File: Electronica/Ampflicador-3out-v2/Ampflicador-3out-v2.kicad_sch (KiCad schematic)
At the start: 28 parts, among them Q1 MPF102, U1 LM386

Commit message: Amp v2
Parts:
- R1, R2, R3, R4, R5, R6: footprint Resistor_THT:R_Axial_DIN0204_L3.6mm_D1.6mm_P5.08mm_Horizontal -> Resistor_THT:R_Axial_DIN0204_L3.6mm_D1.6mm_P7.62mm_Horizontal
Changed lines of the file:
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@@
 			)
 		)
-		(property "Footprint" "Resistor_THT:R_Axial_DIN0204_L3.6mm_D1.6mm_P5.08mm_Horizontal"
+		(property "Footprint" "Resistor_THT:R_Axial_DIN0204_L3.6mm_D1.6mm_P7.62mm_Horizontal"
 			(at 101.346 99.314 90)
 			(effects
@@
 			)
 		)
-		(property "Footprint" "Resistor_THT:R_Axial_DIN0204_L3.6mm_D1.6mm_P5.08mm_Horizontal"
+		(property "Footprint" "Resistor_THT:R_Axial_DIN0204_L3.6mm_D1.6mm_P7.62mm_Horizontal"
 			(at 122.936 105.664 90)
 			(effects
@@
 			)
 		)
-		(property "Footprint" "Resistor_THT:R_Axial_DIN0204_L3.6mm_D1.6mm_P5.08mm_Horizontal"
+		(property "Footprint" "Resistor_THT:R_Axial_DIN0204_L3.6mm_D1.6mm_P7.62mm_Horizontal"
 			(at 36.576 101.854 90)
 			(effects
@@
 			)
 		)
-		(property "Footprint" "Resistor_THT:R_Axial_DIN0204_L3.6mm_D1.6mm_P5.08mm_Horizontal"
+		(property "Footprint" "Resistor_THT:R_Axial_DIN0204_L3.6mm_D1.6mm_P7.62mm_Horizontal"
 			(at 46.736 109.474 90)
 			(effects
@@
 			)
 		)
-		(property "Footprint" "Resistor_THT:R_Axial_DIN0204_L3.6mm_D1.6mm_P5.08mm_Horizontal"
+		(property "Footprint" "Resistor_THT:R_Axial_DIN0204_L3.6mm_D1.6mm_P7.62mm_Horizontal"
 			(at 46.736 75.184 90)
 			(effects
@@
 			)
 		)
-		(property "Footprint" "Resistor_THT:R_Axial_DIN0204_L3.6mm_D1.6mm_P5.08mm_Horizontal"
+		(property "Footprint" "Resistor_THT:R_Axial_DIN0204_L3.6mm_D1.6mm_P7.62mm_Horizontal"
 			(at 54.864 66.294 90)
 			(effects

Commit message: Amp v2 terminada - sin molex
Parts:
- added SW1: SW_DPST_x2, Connector_Molex:Molex_KK-254_AE-6410-02A_1x02_P2.54mm_Vertical, symbol Switch:SW_DPST_x2
- Bass1, Gain1, Output-Jack-6.1, Output-Speaker1, Piezo-Input1, Power-Input1: footprint TerminalBlock_Phoenix:TerminalBlock_Phoenix_MKDS-1,5-2-5.08_1x02_P5.08mm_Horizontal -> Connector_Molex:Molex_KK-254_AE-6410-02A_1x02_P2.54mm_Vertical
- Output-Jack-3.1: footprint Connector_Audio:Jack_3.5mm_CUI_SJ1-3525N_Horizontal -> Connector_Molex:Molex_KK-254_AE-6410-05A_1x05_P2.54mm_Vertical
- Vol1: footprint TerminalBlock_Phoenix:TerminalBlock_Phoenix_MKDS-1,5-3-5.08_1x03_P5.08mm_Horizontal -> Connector_Molex:Molex_KK-254_AE-6410-03A_1x03_P2.54mm_Vertical
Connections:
- net at C1.1, C2.1, C3.2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: now also SW1.2 (B); no longer Power-Input1.2 (Pin_2)
- new net: Power-Input1.2 (Pin_2), SW1.1 (A)
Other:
- moved on the sheet: Bass1, C1, C10, C11, C12, C2, C3, C4, C5, C6, C7, C8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

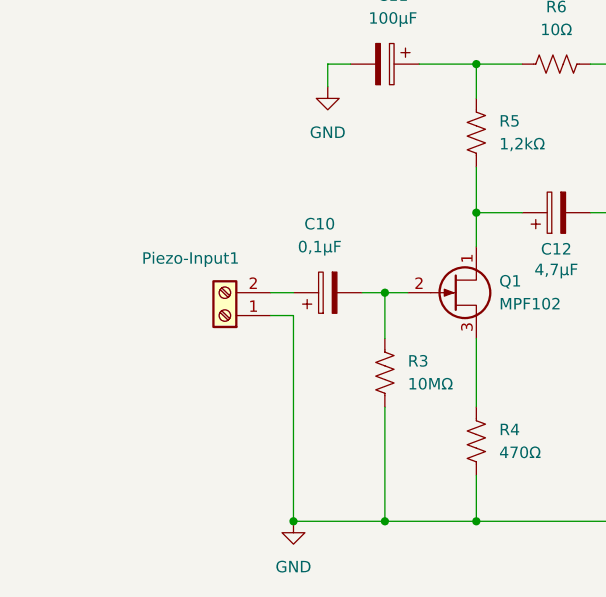
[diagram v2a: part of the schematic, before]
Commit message: PCB Amp v2 terminada - Molex
Plano de masa
Conectores Molex
3 piezos
Suma de señales de entrada
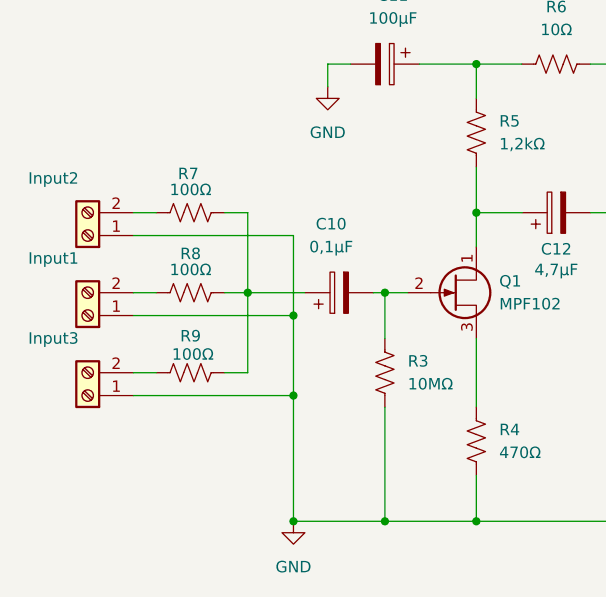
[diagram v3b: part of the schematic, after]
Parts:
- added Input2, Input3: Screw_Terminal_01x02, Connector_Molex:Molex_KK-254_AE-6410-02A_1x02_P2.54mm_Vertical, symbol Connector:Screw_Terminal_01x02
- added R7, R8, R9: 100Ω, Resistor_THT:R_Axial_DIN0204_L3.6mm_D1.6mm_P7.62mm_Horizontal, symbol Device:R_US
- renumbered Piezo-Input1 to Input1
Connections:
- net GND: now also Input2.1 (Pin_1), Input3.1 (Pin_1)
- net at C10.1: now also R7.2, R8.2, R9.2; no longer Input1.2 (Pin_2)
- new net: Input2.2 (Pin_2), R7.1
- new net: Input3.2 (Pin_2), R9.1
- new net: Input1.2 (Pin_2), R8.1
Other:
- moved on the sheet: C10, Input1
